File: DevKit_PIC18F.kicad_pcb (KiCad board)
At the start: 2 copper layers, 41 x 72 mm, 29 parts, among them J1 PIC_ICSP_ICD, J2 USB_B, J3 5P_UART, J4 RA_PORT, J5 RB_PORT, J6 RD_PORT, J7 RC_PORT, J8 RE_PORT, SW1 SW_RST, X1 16MHz

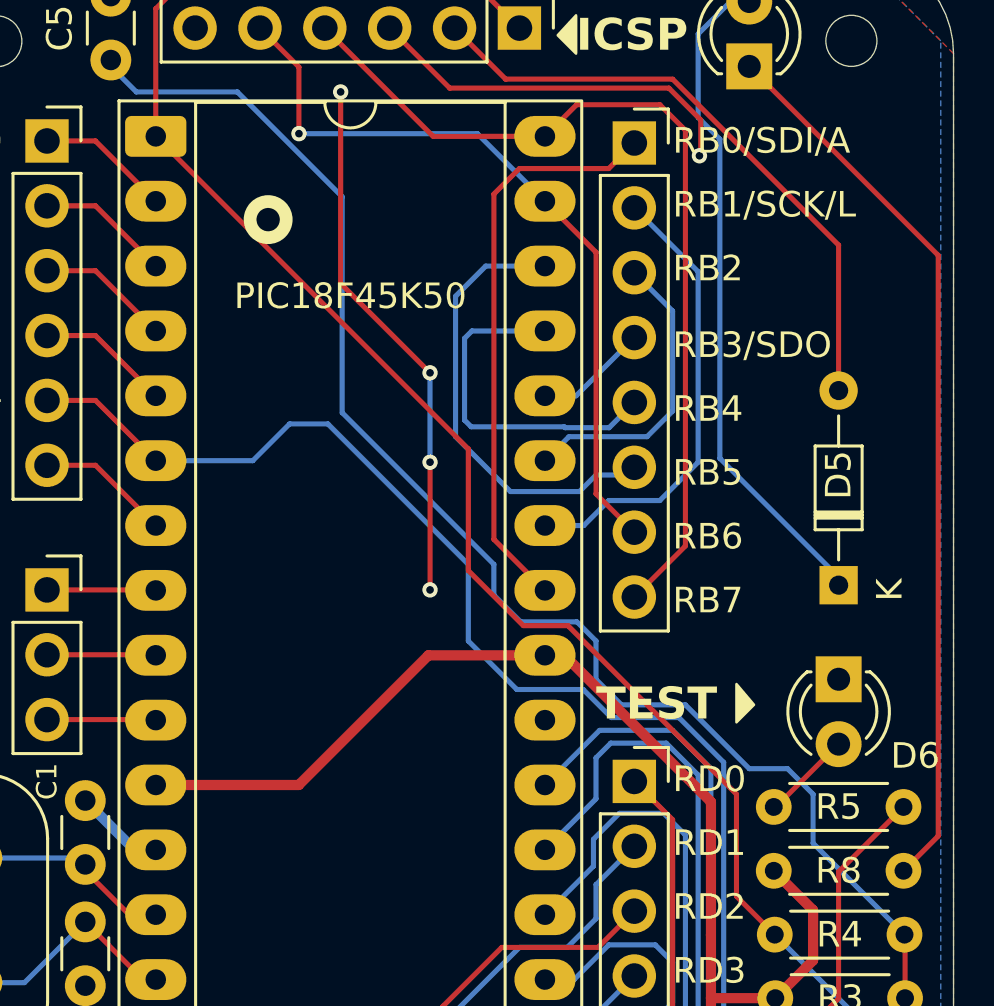
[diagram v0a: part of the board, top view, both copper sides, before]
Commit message: Fix PWR_Flag & GND on PCB
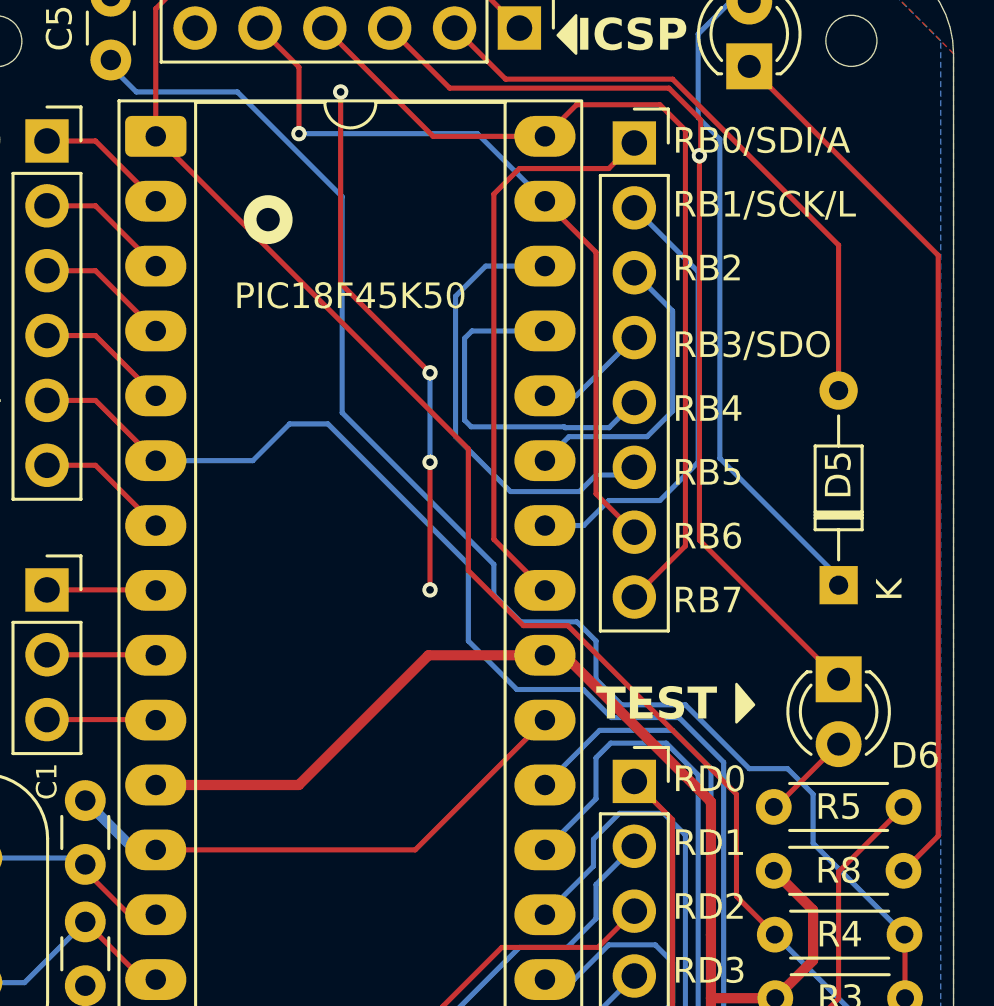
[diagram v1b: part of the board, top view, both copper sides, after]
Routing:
- net GND: track 40.7 -> 80.8 mm
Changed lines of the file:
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@@
 	(paper "A5")
 	(title_block
-		(comment 1 "Rev.3 : Remove bridge & re-route to fix USB-B power.")
-		(comment 2 "Rev.4 : Add Test LED, flip ICSP + move LED, Group all Resistors.")
+		(comment 1 "Rev.7 : Upgrade -> KiCAD 9.0.0 & fix GND & PWR_Flag.")
+		(comment 2 "Rev.6 : Fix LED D6 -> GND instead of pull-up VCC.")
 		(comment 3 "Rev.5 : Remove redundant LED D1.")
-		(comment 4 "Rev.6 : Fix LED D6 -> GND instead of pull-up VCC.")
-		(comment 5 "Rev.7 : Upgrade -> KiCAD 9.0.0 & fix GND.")
+		(comment 4 "Rev.4 : Add Test LED, flip ICSP + move LED, Group all Resistors.")
+		(comment 5 "Rev.3 : Remove bridge & re-route to fix USB-B power.")
 	)
 	(layers
@@
 		)
 		(property ki_fp_filters "PinHeader*1x06*P2.54mm* PinSocket*1x06*P2.54mm*")
-		(sheetname "Root")
+		(sheetname "/")
 		(sheetfile "DevKit_PIC18F.kicad_sch")
 		(attr through_hole)
@@
 		)
 		(property ki_fp_filters "R_*")
-		(sheetname "Root")
+		(sheetname "/")
 		(sheetfile "DevKit_PIC18F.kicad_sch")
 		(attr through_hole)
@@
 		)
 		(property ki_fp_filters "C_*")
-		(sheetname "Root")
+		(sheetname "/")
 		(sheetfile "DevKit_PIC18F.kicad_sch")
 		(attr through_hole)
@@
 			)
 		)
+		(property "Sim.Pins" "1=K 2=A"
+			(at 0 0 270)
+			(unlocked yes)
+			(layer "F.Fab")
+			(hide yes)
+			(effects
+				(font
+					(size 1 1)
+					(thickness 0.15)
+				)
+			)
+		)
 		(property ki_fp_filters "LED* LED_SMD:* LED_THT:*")
-		(sheetname "Root")
+		(sheetname "/")
 		(sheetfile "DevKit_PIC18F.kicad_sch")
 		(attr through_hole)
@@
 		)
 		(property ki_fp_filters "Connector*:*_1x??_*")
-		(sheetname "Root")
+		(sheetname "/")
 		(sheetfile "DevKit_PIC18F.kicad_sch")
 		(attr through_hole)
@@
 		)
 		(property ki_fp_filters "Connector*:*_1x??_*")
-		(sheetname "Root")
+		(sheetname "/")
 		(sheetfile "DevKit_PIC18F.kicad_sch")
 		(attr through_hole)
@@
 			)
 		)
+		(property "Sim.Pins" "1=K 2=A"
+			(at 0 0 90)
+			(unlocked yes)
+			(layer "F.Fab")
+			(hide yes)
+			(effects
+				(font
+					(size 1 1)
+					(thickness 0.15)
+				)
+			)
+		)
 		(property ki_fp_filters "LED* LED_SMD:* LED_THT:*")
-		(sheetname "Root")
+		(sheetname "/")
 		(sheetfile "DevKit_PIC18F.kicad_sch")
 		(attr through_hole)
@@
 		)
 		(property ki_fp_filters "Connector*:*_1x??_*")
-		(sheetname "Root")
+		(sheetname "/")
 		(sheetfile "DevKit_PIC18F.kicad_sch")
 		(attr through_hole)
@@
 		)
 		(property ki_fp_filters "PDIP40_P_MCH")
-		(sheetname "Root")
+		(sheetname "/")
 		(sheetfile "DevKit_PIC18F.kicad_sch")
 		(attr through_hole)
@@
 			(net 9 "/MCLR")
 			(pinfunction "RE3/VPP/*MCLR")
-			(pintype "power_in")
+			(pintype "input")
 		)
 		(pad "2" thru_hole oval
@@
 		)
 		(property ki_fp_filters "C_*")
-		(sheetname "Root")
+		(sheetname "/")
 		(sheetfile "DevKit_PIC18F.kicad_sch")
 		(attr through_hole)
@@
 		)
 		(property ki_fp_filters "Crystal*")
-		(sheetname "Root")
+		(sheetname "/")
 		(sheetfile "DevKit_PIC18F.kicad_sch")
 		(attr through_hole)
@@
 		)
 		(property ki_fp_filters "TO-???* *_Diode_* *SingleDiode* D_*")
-		(sheetname "Root")
+		(sheetname "/")
 		(sheetfile "DevKit_PIC18F.kicad_sch")
 		(attr through_hole)
@@
 		)
 		(property ki_fp_filters "Connector*:*_1x??_*")
-		(sheetname "Root")
+		(sheetname "/")
 		(sheetfile "DevKit_PIC18F.kicad_sch")
 		(attr through_hole)
@@
 		)
 		(property ki_fp_filters "C_*")
-		(sheetname "Root")
+		(sheetname "/")
 		(sheetfile "DevKit_PIC18F.kicad_sch")
 		(attr through_hole)
@@
 		)
 		(property ki_fp_filters "C_*")
-		(sheetname "Root")
+		(sheetname "/")
 		(sheetfile "DevKit_PIC18F.kicad_sch")
 		(attr through_hole)
@@
 		)
 		(property ki_fp_filters "C_*")
-		(sheetname "Root")
+		(sheetname "/")
 		(sheetfile "DevKit_PIC18F.kicad_sch")
 		(attr through_hole)
@@
 			)
 		)
+		(property "Sim.Pins" "1=K 2=A"
+			(at 0 0 0)
+			(unlocked yes)
+			(layer "F.Fab")
+			(hide yes)
+			(effects
+				(font
+					(size 1 1)
+					(thickness 0.15)
+				)
+			)
+		)
 		(property ki_fp_filters "LED* LED_SMD:* LED_THT:*")
-		(sheetname "Root")
+		(sheetname "/")
 		(sheetfile "DevKit_PIC18F.kicad_sch")
 		(attr through_hole)
@@
 		)
 		(property ki_fp_filters "SW?DIP?x1*")
-		(sheetname "Root")
+		(sheetname "/")
 		(sheetfile "DevKit_PIC18F.kicad_sch")
 		(attr through_hole)
@@
 		)
 		(property ki_fp_filters "USB*")
-		(sheetname "Root")
+		(sheetname "/")
 		(sheetfile "DevKit_PIC18F.kicad_sch")
 		(attr through_hole)
@@
 		)
 		(property ki_fp_filters "TO-???* *_Diode_* *SingleDiode* D_*")
-		(sheetname "Root")
+		(sheetname "/")
 		(sheetfile "DevKit_PIC18F.kicad_sch")
 		(attr through_hole)
@@
 		)
 		(property ki_fp_filters "R_*")
-		(sheetname "Root")
+		(sheetname "/")
 		(sheetfile "DevKit_PIC18F.kicad_sch")
 		(attr through_hole)
@@
 		)
 		(property ki_fp_filters "Connector*:*_1x??_*")
-		(sheetname "Root")
+		(sheetname "/")
 		(sheetfile "DevKit_PIC18F.kicad_sch")
 		(attr through_hole)
@@
 		)
 		(property ki_fp_filters "C_*")
-		(sheetname "Root")
+		(sheetname "/")
 		(sheetfile "DevKit_PIC18F.kicad_sch")
 		(attr through_hole)
@@
 		)
 		(property ki_fp_filters "R_*")
-		(sheetname "Root")
+		(sheetname "/")
 		(sheetfile "DevKit_PIC18F.kicad_sch")
 		(attr through_hole)
@@
 		)
 		(property ki_fp_filters "R_*")
-		(sheetname "Root")
+		(sheetname "/")
 		(sheetfile "DevKit_PIC18F.kicad_sch")
 		(attr through_hole)
@@
 		)
 		(property ki_fp_filters "C_*")
-		(sheetname "Root")
+		(sheetname "/")
 		(sheetfile "DevKit_PIC18F.kicad_sch")
 		(attr through_hole)
@@
 		)
 		(property ki_fp_filters "Connector*:*_1x??_*")
-		(sheetname "Root")
+		(sheetname "/")
 		(sheetfile "DevKit_PIC18F.kicad_sch")
 		(attr through_hole)
@@
 		)
 		(property ki_fp_filters "R_*")
-		(sheetname "Root")
+		(sheetname "/")
 		(sheetfile "DevKit_PIC18F.kicad_sch")
 		(attr through_hole)
@@
 		)
 		(property ki_fp_filters "R_*")
-		(sheetname "Root")
+		(sheetname "/")
 		(sheetfile "DevKit_PIC18F.kicad_sch")
 		(attr through_hole)
@@
 	)
 	(segment
+		(start 99.05 49.55)
+		(end 99.05 34.5)
+		(width 0.2)
+		(layer "F.Cu")
+		(net 2)
+	)
+	(segment
 		(start 85 39.5)
 		(end 88.5 43)
@@
 	)
 	(segment
+		(start 104.5 55)
+		(end 99.05 49.55)
+		(width 0.2)
+		(layer "F.Cu")
+		(net 2)
+	)
+	(segment
 		(start 88.5 46.5)
 		(end 88.5 51.5)
@@
 	)
 	(segment
+		(start 87.92 61.68)
+		(end 77.76 61.68)
+		(width 0.2)
+		(layer "F.Cu")
+		(net 2)
+	)
+	(segment
 		(start 99.099609 34.450391)
 		(end 99.099609 33.095997)
 		(width 0.2)
 		(layer "F.Cu")
+		(net 2)
+	)
+	(segment
+		(start 93 56.6)
+		(end 87.92 61.68)
+		(width 0.2)
+		(layer "F.Cu")

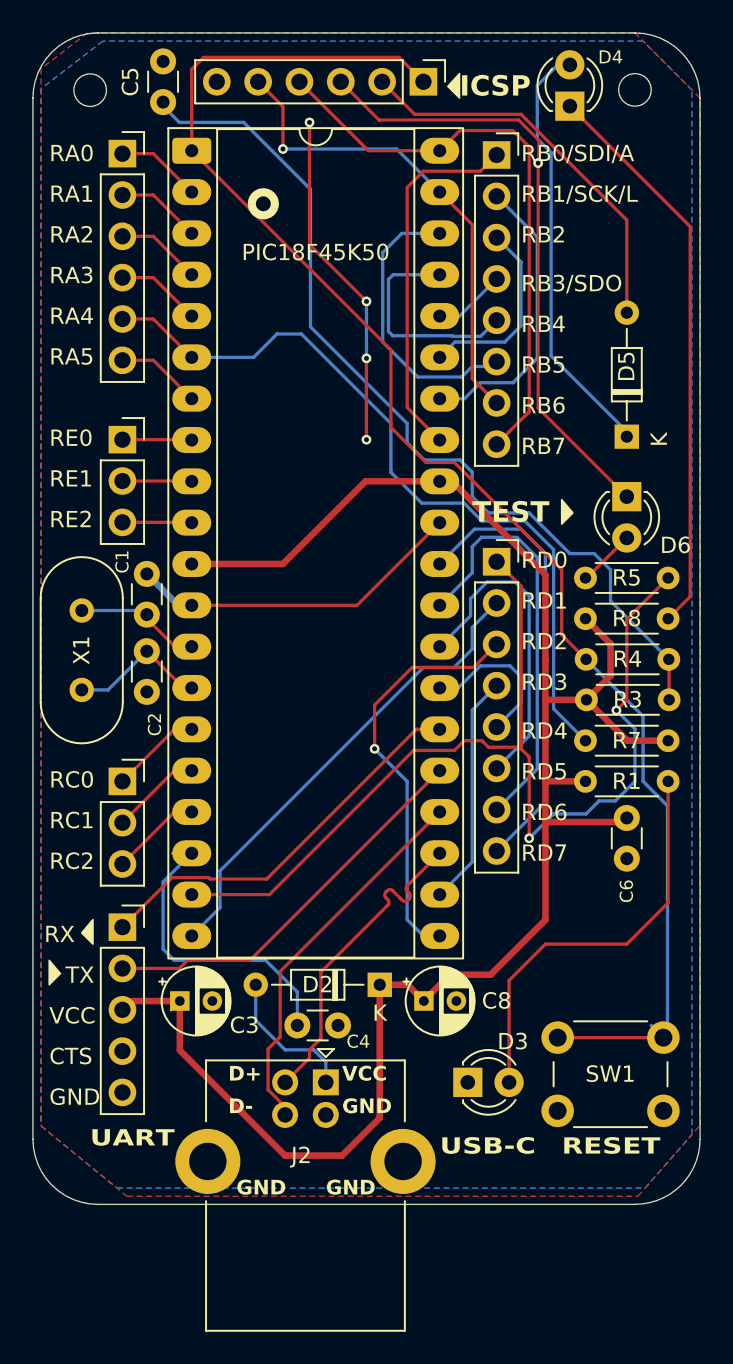
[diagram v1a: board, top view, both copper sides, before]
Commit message: Update Rev.8: Fix SCH bug, remove D/R/L from ISCP & D6->RA0
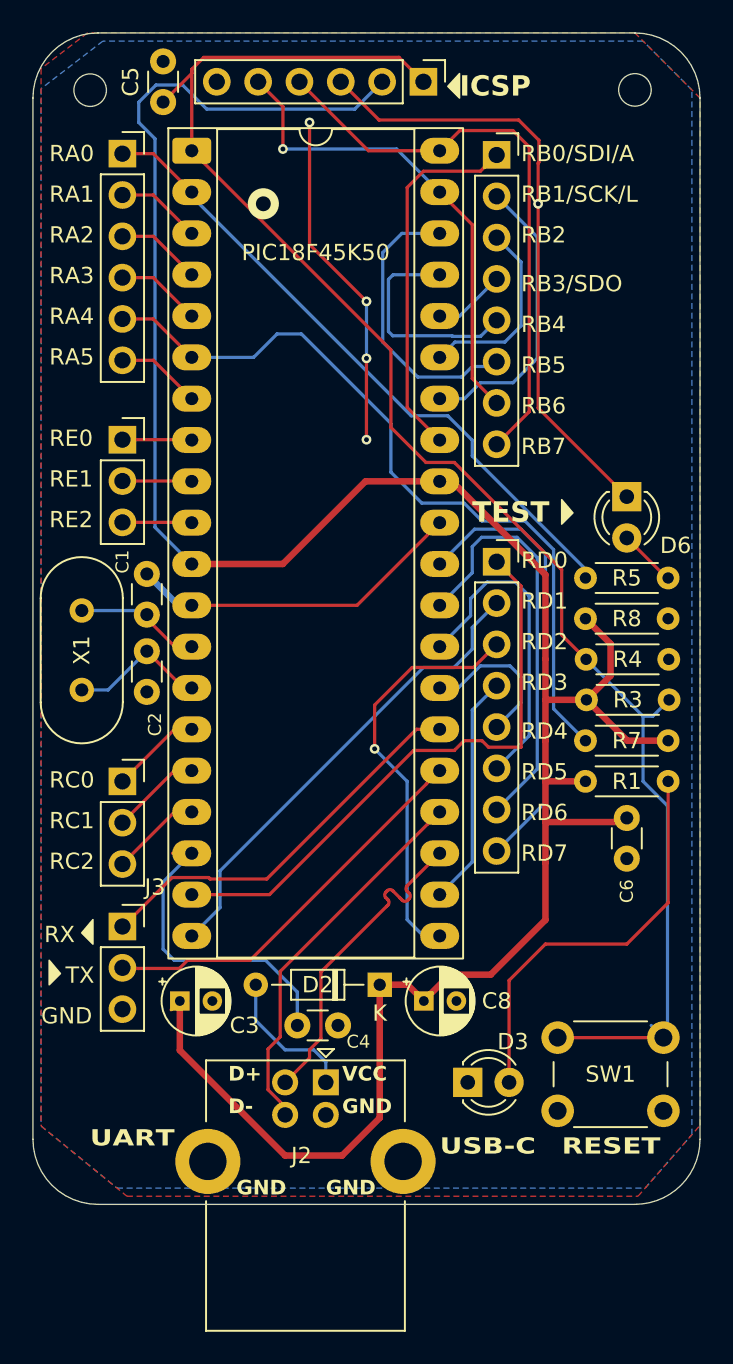
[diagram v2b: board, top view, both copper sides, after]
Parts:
- removed D4: LED_VDD, LED_THT:LED_D3.0mm_FlatTop
- removed D5: D_Schottky, Diode_THT:D_DO-34_SOD68_P7.62mm_Horizontal
- C5: value 10uF -> 1uF
- J3: footprint Connector_PinSocket_2.54mm:PinSocket_1x05_P2.54mm_Vertical -> Connector_PinSocket_2.54mm:PinSocket_1x03_P2.54mm_Vertical
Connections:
- C5 pad 2: Net-(C5-Pad2) -> /MCLR
- J1 pad 2: Net-(D5-A) -> VCC
- J3 pad 3: VCC -> GND
- R3 pad 2: Net-(C5-Pad2) -> /MCLR
- R5 pad 1: Net-(J6-Pin_1) -> Net-(D6-A)
- R5 pad 2: Net-(D6-A) -> Net-(J4-Pin_1)
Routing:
- net Net-(C5-Pad2): track 55.3 -> 0.03 mm
- net VCC: track 115.5 -> 157.7 mm
- net Net-(J4-Pin_1): track 5.77 -> 40.9 mm
- net Net-(D4-K): track 35.1 -> 0.00 mm
- net Net-(J6-Pin_1): track 65.4 -> 36.3 mm, vias 2 -> 0
- net Net-(D4-A): track 26.4 -> 0.00 mm
- net Net-(D5-A): track 24.3 -> 0.00 mm
- net /MCLR: track 95.8 -> 100.6 mm
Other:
- board text added: "DevKit PIC18F45XX Rev.8 : 2nd April, 2025 Designed by @deulamco"
- board text removed: "CTS"
- board text removed: "DevKit PIC18F45XX Rev.7 : 28th Feb, 2025 Designed by @deulamco"
